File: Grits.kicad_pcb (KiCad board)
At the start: 2 copper layers, 56 x 22 mm, 64 parts, among them J1 Conn_01x06_MountingPin, J2 Conn_02x01, J3 Conn_ARM_JTAG_SWD_10, J4 Conn_01x03, J5 Conn_01x04_MountingPin, J6 Conn_01x04_MountingPin, Q1 BUK7M9R9-60E, Q2 BUK7M9R9-60E, Q3 BUK7M9R9-60E, Q4 BUK7M9R9-60E, Q5 BUK7M9R9-60E, Q6 BUK7M9R9-60E, U1 STSPIN32F0B

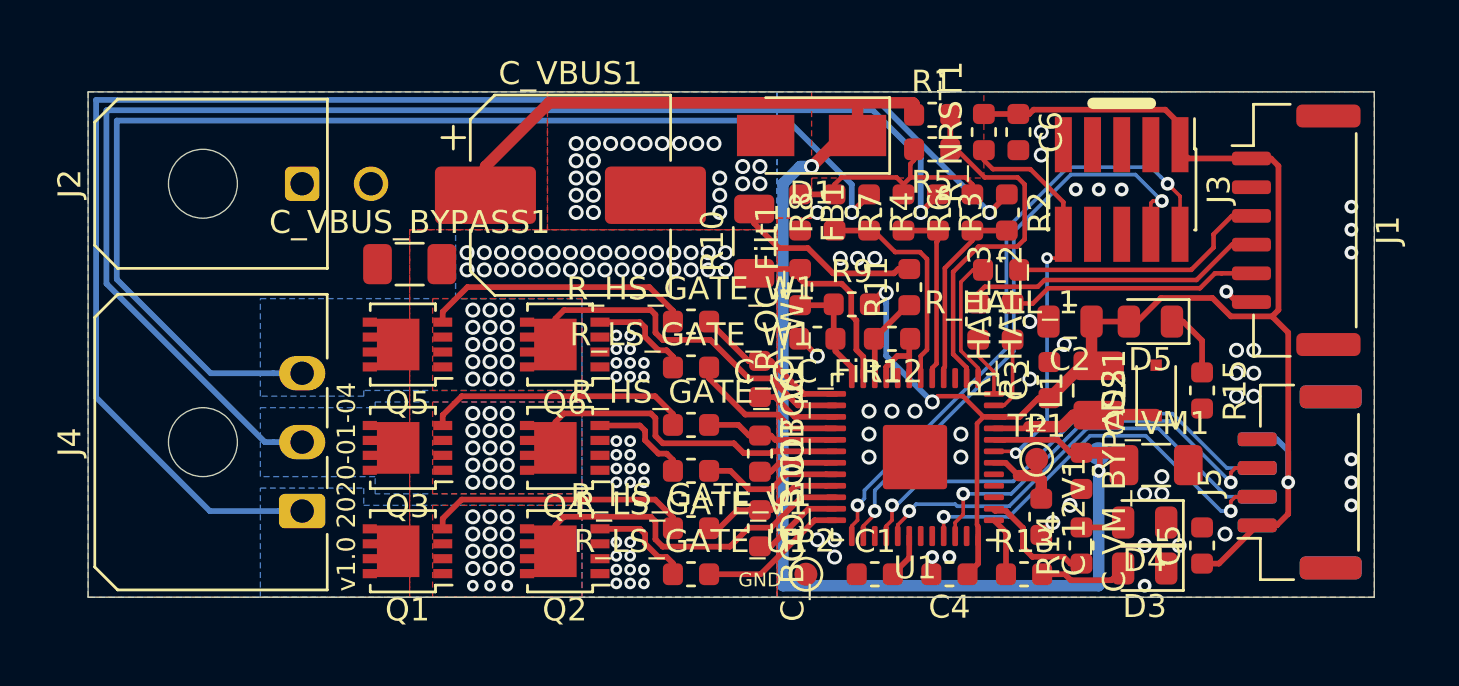
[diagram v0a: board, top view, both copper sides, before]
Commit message: ✨ Add v1.1
Featuring rotated Hall connector going to different timer inputs
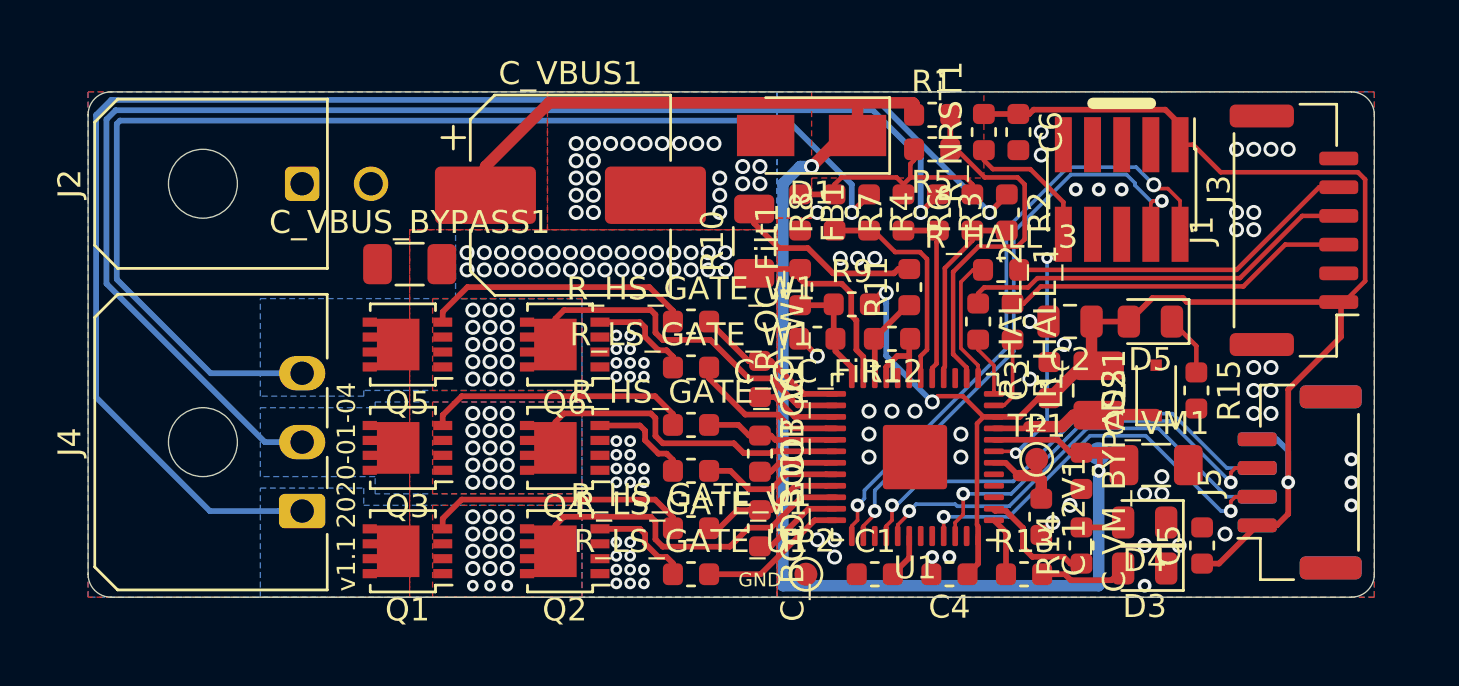
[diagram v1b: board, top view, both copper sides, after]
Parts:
- C_12V1: value 2.2µF -> 2.2µF/16V
- moved R_HALL_1 2.30 mm to (145.2, 104.0), turned to 270 degrees
- moved R_HALL_3 2.30 mm to (144.8, 101.8), turned to 0 degrees
- moved R15 0.25 mm to (153.2, 107.0)
- moved J1 0.10 mm to (157.5, 100.0), turned to 90 degrees
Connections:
- U1 pad 11: /HALL_3_R -> /HALL_1_R
- U1 pad 13: /HALL_1_R -> /HALL_3_R
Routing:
- net VDD: track 70.7 -> 77.8 mm
- net /HALL_3: track 10.9 -> 15.4 mm
- net /HALL_2: track 13.2 -> 17.5 mm
- net /HALL_1: track 11.4 -> 15.3 mm
- net /HALL_3_R: track 3.46 -> 5.68 mm
- net /HALL_1_R: track 5.68 -> 3.46 mm
- net GND: track 2.38 -> 1.10 mm, vias 47 -> 51
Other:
- outline, holes or cut-outs redrawn
- board text added: "v1.1 2020-01-04"
- board text removed: "v1.0 2020-01-04"

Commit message: ✨ Add v1.3a (DFM)
v1.2: Retooled for DFM through JLCPCB
v1.3: Fix bootstrap capacitor wiring error
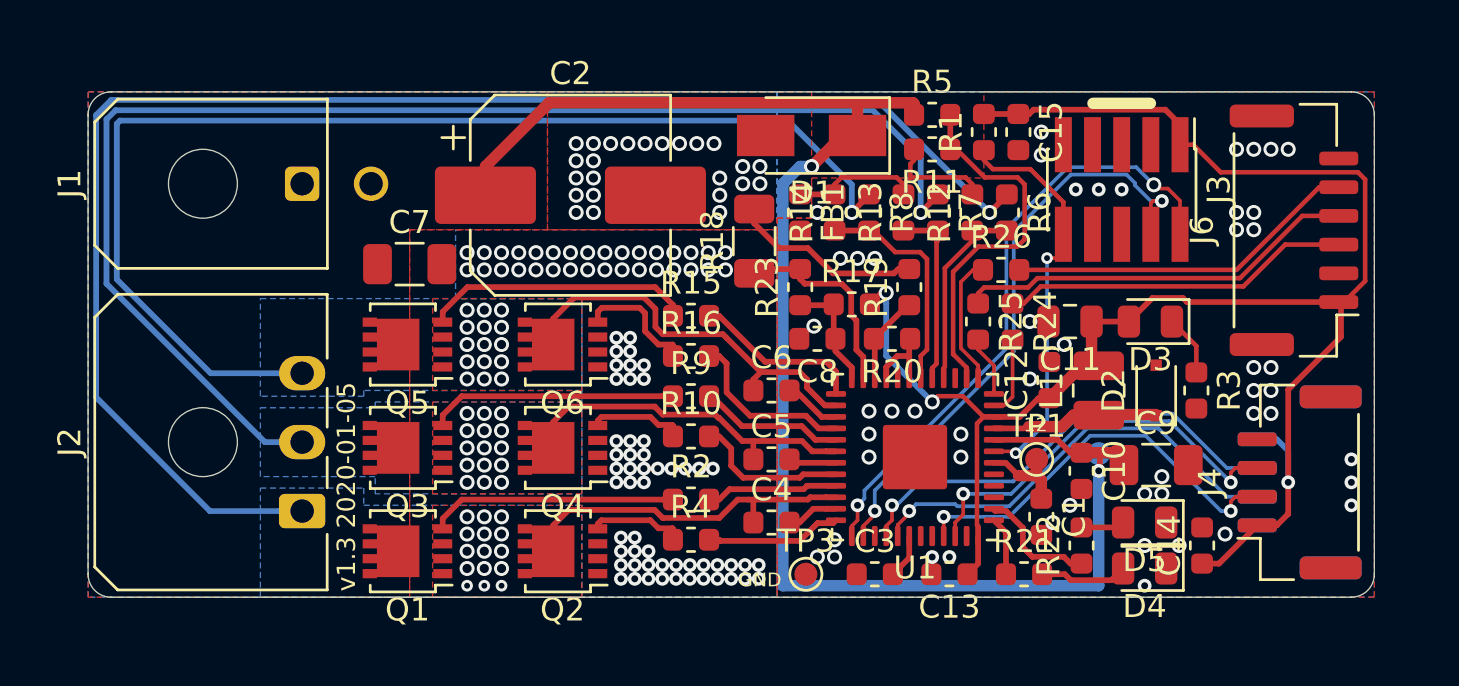
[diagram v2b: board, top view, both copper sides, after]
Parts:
- removed C_BOOT_U1, C_BOOT_V1: 100nF, Capacitor_SMD:C_0603_1608Metric
- removed the D3 at (151.0, 114.8)
- removed R_LS_GATE_V1: 5R, Resistor_SMD:R_0603_1608Metric
- added C4: 100nF 50V X7R, Capacitor_SMD:C_0603_1608Metric, F.Cu at (134.8, 112.8)
- added C5: 100nF 50V X7R, Capacitor_SMD:C_0603_1608Metric, F.Cu at (134.8, 110.0)
- added D4: RED 红, LED_SMD:LED_0805_2012Metric, F.Cu at (151.0, 114.8)
- added R10: 5.1Ω, Resistor_SMD:R_0603_1608Metric, F.Cu at (131.2, 109.0)
- C1: renamed from C_12V1; value 2.2µF/16V -> 2.2µF 16V
- C10: renamed from C_VM_BYPASS1; value 100nF/50V -> 100nF 50V X7R
- C11: renamed from C2; value 47µF -> 47µF 6.3V
- C12: renamed from C3; value 100nF -> 100nF 50V X7R
- C13: renamed from C4; value 100nF -> 100nF 50V X7R
- C14: renamed from C5; value 100nF -> 100nF 50V X7R
- C15: renamed from C6; value 100nF -> 100nF 50V X7R
- C2: renamed from C_VBUS1; value 150µF/50V -> 220µF 35V
- C3: renamed from C1; value 100nF -> 100nF 50V X7R
- C6: renamed from C_BOOT_W1; value 100nF -> 100nF 50V X7R
- C7: renamed from C_VBUS_BYPASS1; value 10uF/50V -> 10µF 50V
- C9: renamed from C_VM1; value 10µF/50V -> 10µF 50V
- D1: value SMAJ43A -> SMAJ33A
- D2: value DB2J50100L -> PMEG6010CEJ,115 DB2J50100L
- D3: renamed from D5; value LED -> GREEN 绿
- D5: renamed from D4; value LED -> YELLOW 黄
- J3: value Conn_ARM_JTAG_SWD_10 -> FTSH-105-01-F-DV
- R1: renamed from R_NRST1; value 22k -> 22kΩ
- R11: renamed from R5; value 10k -> 20kΩ 1%
- R12: renamed from R6; value 10k -> 20kΩ 1%
- R13: renamed from R7; value 10k -> 20kΩ 1%
- R14: renamed from R8; value 10k -> 20kΩ 1%
- R15: renamed from R_HS_GATE_W1; value 5R -> 5.1Ω
- R16: renamed from R_LS_GATE_W1; value 5R -> 5.1Ω
- R18: renamed from R10; value 10mR -> 10mΩ 1W
- R19: renamed from R11; value 105k/0.5% -> 150kΩ 0.5%
- R2: renamed from R_HS_GATE_U1; value 5R -> 5.1Ω
- R20: renamed from R12; value 7.5k/0.5% -> 10kΩ 0.5%
- R21: renamed from R13; value 3.3k -> 3.3kΩ
- R22: renamed from R14; value 3.3k -> 3.3kΩ
- R23: renamed from R_OC_Filt1; value 1.5k -> 1.5kΩ
- R24: renamed from R_HALL_1; value 22R -> 22Ω
- R25: renamed from R_HALL_2; value 22R -> 22Ω
- R26: renamed from R_HALL_3; value 22R -> 22Ω
- R3: renamed from R15; value 3.3k -> 3.3kΩ
- R4: renamed from R_LS_GATE_U1; value 5R -> 5.1Ω
- R5: renamed from R1; value 110k -> 220kΩ 1%
- R6: renamed from R2; value 110k -> 220kΩ 1%
- R7: renamed from R3; value 110k -> 220kΩ 1%
- R8: renamed from R4; value 110k -> 220kΩ 1%
- R9: renamed from R_HS_GATE_V1; value 5R -> 5.1Ω
- moved R4 1.50 mm to (131.2, 113.5)
- moved R2 1.25 mm to (131.2, 111.8)
- moved R9 1.25 mm to (131.2, 107.2)
- moved C6 0.71 mm to (134.8, 107.0), turned to 0 degrees
- moved R16 0.50 mm to (131.2, 105.5)
- moved R15 0.25 mm to (131.2, 103.8)
- moved Q2 0.09 mm to (125.7, 114.0)
- moved Q4 0.09 mm to (125.7, 109.5)
- moved Q6 0.09 mm to (125.7, 105.0)
- renumbered C_OC_Filt1 to C8, J2 to J1, J4 to J2, J5 to J4, J6 to J5, J1 to J6, R9 to R17, TP3 to TP2, TP2 to TP3
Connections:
- C6 pad 1: /HS_GATE_W -> /PHASE_W
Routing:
- net /INVERTER_SRC: track 8.92 -> 12.5 mm, vias 62 -> 86
- net /BOOT_U: track 3.99 -> 2.27 mm
- net /PHASE_W: track 67.7 -> 69.4 mm
- net /BOOT_V: track 3.47 -> 2.09 mm
- net /BOOT_W: track 3.67 -> 2.50 mm
- net GND: track 1.10 -> 0.04 mm
- net /LS_GATE_W_R: track 4.52 -> 5.40 mm
- net /HS_GATE_V_R: track 11.6 -> 10.8 mm
- net /HS_GATE_U_R: track 11.6 -> 10.8 mm
- net /HS_GATE_W: track 6.83 -> 7.50 mm
- net /LS_GATE_W: track 6.90 -> 7.57 mm
- net /LS_GATE_V: track 6.13 -> 6.78 mm
- net /PHASE_V: track 73.2 -> 73.8 mm
- net /LS_GATE_U: track 6.50 -> 5.92 mm
- net /HS_GATE_U: track 6.29 -> 5.77 mm
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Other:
- board text added: "v1.3 2020-01-05"
- board text removed: "v1.1 2020-01-04"
